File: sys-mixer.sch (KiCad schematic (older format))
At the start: 11 parts, among them J1 RCA L&R, J2 RCA L&R, J3 RCA L&R, SW1 4PDT

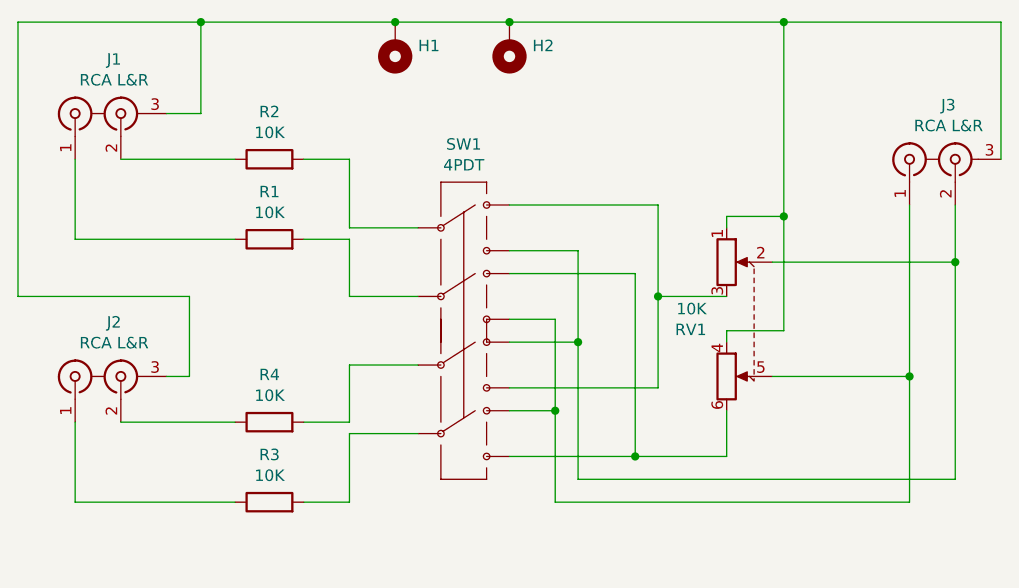
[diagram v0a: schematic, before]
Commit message: Fix resistor position in schematic
Having the resistors right after the inputs causes the mixing to
misbehave.

Also tweaked mounting hole and control positions, based on fitting of
2019-01-15 boards.
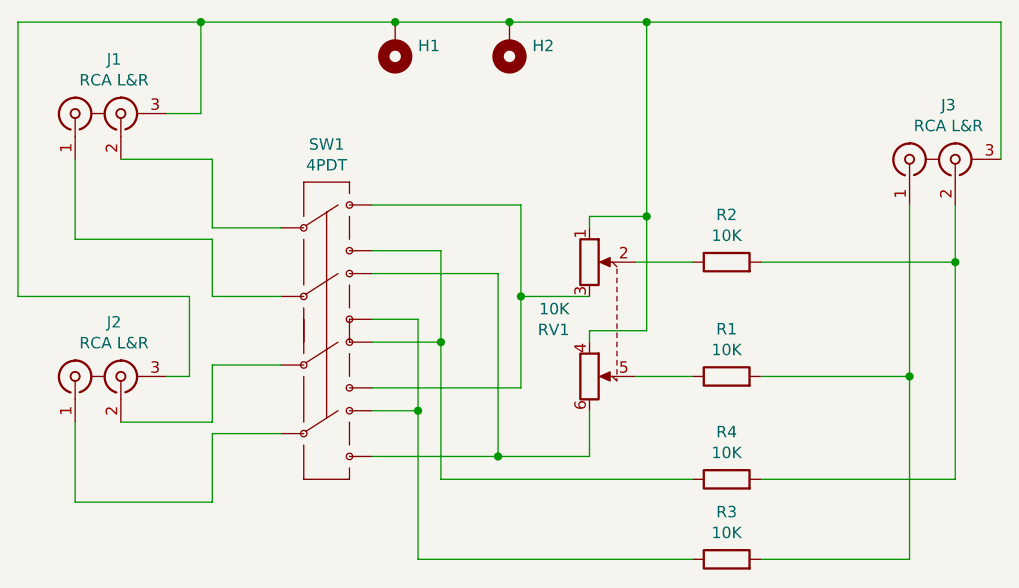
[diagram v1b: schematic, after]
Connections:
- net at J1.1 (IN1): now also SW1.6; no longer R1.1
- net at J1.2 (IN2): now also SW1.3; no longer R2.1
- net at J2.1 (IN1): now also SW1.12; no longer R3.1
- net at J2.2 (IN2): now also SW1.9; no longer R4.1
- net at SW1.10, SW1.5: now also R3.1; no longer J3.1 (IN1), RV1.5
- net at SW1.2, SW1.7: now also R4.1; no longer J3.2 (IN2), RV1.2
- net at R2.2: now also J3.2 (IN2), R4.2; no longer SW1.3
- net at R1.2: now also J3.1 (IN1), R3.2; no longer SW1.6
- new net: R2.1, RV1.2
- new net: R1.1, RV1.5
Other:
- moved on the sheet: R1, R2, R3, R4, RV1, SW1
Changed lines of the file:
@@
 EESchema Schematic File Version 4
+LIBS:sys-mixer-cache
 EELAYER 26 0
 EELAYER END
@@
 Sheet 1 1
 Title "SYS Mixer"
-Date "2019-01-15"
+Date "2019-01-26"
 Rev "0"
 Comp "Guano Audio Technologies"
@@
 L Device:R R2
 U 1 1 5C3BB760
-P 1900 1650
-F 0 "R2" V 2107 1650 50  0000 C CNN
-F 1 "10K" V 2016 1650 50  0000 C CNN
-F 2 "Resistor_THT:R_Axial_DIN0207_L6.3mm_D2.5mm_P10.16mm_Horizontal" V 1830 1650 50  0001 C CNN
-F 3 "/home/alex/Documents/pcb/sys-mixer/datasheets/mrs16m25-239694.pdf" H 1900 1650 50  0001 C CNN
-	1    1900 1650
+P 3900 2100
+F 0 "R2" V 4107 2100 50  0000 C CNN
+F 1 "10K" V 4016 2100 50  0000 C CNN
+F 2 "Resistor_THT:R_Axial_DIN0207_L6.3mm_D2.5mm_P10.16mm_Horizontal" V 3830 2100 50  0001 C CNN
+F 3 "/home/alex/Documents/pcb/sys-mixer/datasheets/mrs16m25-239694.pdf" H 3900 2100 50  0001 C CNN
+	1    3900 2100
 	0    -1   -1   0
 $EndComp
@@
 L Device:R R1
 U 1 1 5C3BB7F1
-P 1900 2000
-F 0 "R1" V 2107 2000 50  0000 C CNN
-F 1 "10K" V 2016 2000 50  0000 C CNN
-F 2 "Resistor_THT:R_Axial_DIN0207_L6.3mm_D2.5mm_P10.16mm_Horizontal" V 1830 2000 50  0001 C CNN
-F 3 "/home/alex/Documents/pcb/sys-mixer/datasheets/mrs16m25-239694.pdf" H 1900 2000 50  0001 C CNN
-	1    1900 2000
+P 3900 2600
+F 0 "R1" V 4107 2600 50  0000 C CNN
+F 1 "10K" V 4016 2600 50  0000 C CNN
+F 2 "Resistor_THT:R_Axial_DIN0207_L6.3mm_D2.5mm_P10.16mm_Horizontal" V 3830 2600 50  0001 C CNN
+F 3 "/home/alex/Documents/pcb/sys-mixer/datasheets/mrs16m25-239694.pdf" H 3900 2600 50  0001 C CNN
+	1    3900 2600
 	0    -1   -1   0
 $EndComp
@@
 L Device:R R4
 U 1 1 5C3BBB9D
-P 1900 2800
-F 0 "R4" V 2107 2800 50  0000 C CNN
-F 1 "10K" V 2016 2800 50  0000 C CNN
-F 2 "Resistor_THT:R_Axial_DIN0207_L6.3mm_D2.5mm_P10.16mm_Horizontal" V 1830 2800 50  0001 C CNN
-F 3 "/home/alex/Documents/pcb/sys-mixer/datasheets/mrs16m25-239694.pdf" H 1900 2800 50  0001 C CNN
-	1    1900 2800
+P 3900 3050
+F 0 "R4" V 4107 3050 50  0000 C CNN
+F 1 "10K" V 4016 3050 50  0000 C CNN
+F 2 "Resistor_THT:R_Axial_DIN0207_L6.3mm_D2.5mm_P10.16mm_Horizontal" V 3830 3050 50  0001 C CNN
+F 3 "/home/alex/Documents/pcb/sys-mixer/datasheets/mrs16m25-239694.pdf" H 3900 3050 50  0001 C CNN
+	1    3900 3050
 	0    -1   -1   0
 $EndComp
@@
 L Device:R R3
 U 1 1 5C3BBBA4
-P 1900 3150
-F 0 "R3" V 2107 3150 50  0000 C CNN
-F 1 "10K" V 2016 3150 50  0000 C CNN
-F 2 "Resistor_THT:R_Axial_DIN0207_L6.3mm_D2.5mm_P10.16mm_Horizontal" V 1830 3150 50  0001 C CNN
-F 3 "/home/alex/Documents/pcb/sys-mixer/datasheets/mrs16m25-239694.pdf" H 1900 3150 50  0001 C CNN
-	1    1900 3150
+P 3900 3400
+F 0 "R3" V 4107 3400 50  0000 C CNN
+F 1 "10K" V 4016 3400 50  0000 C CNN
+F 2 "Resistor_THT:R_Axial_DIN0207_L6.3mm_D2.5mm_P10.16mm_Horizontal" V 3830 3400 50  0001 C CNN
+F 3 "/home/alex/Documents/pcb/sys-mixer/datasheets/mrs16m25-239694.pdf" H 3900 3400 50  0001 C CNN
+	1    3900 3400
 	0    -1   -1   0
 $EndComp
@@
 L Device:R_POT_Dual RV1
 U 1 1 5C3BC3EF
-P 4000 2350
-F 0 "RV1" V 4046 2162 50  0000 R CNN
-F 1 "10K" V 3955 2162 50  0000 R CNN
-F 2 "extra-footprints:POT-RK09712200MC" H 4250 2275 50  0001 C CNN
-F 3 "/home/alex/Documents/pcb/sys-mixer/datasheets/RK097-1370742.pdf" H 4250 2275 50  0001 C CNN
-	1    4000 2350
+P 3400 2350
+F 0 "RV1" V 3446 2162 50  0000 R CNN
+F 1 "10K" V 3355 2162 50  0000 R CNN
+F 2 "extra-footprints:POT-RK09712200MC" H 3650 2275 50  0001 C CNN
+F 3 "/home/alex/Documents/pcb/sys-mixer/datasheets/RK097-1370742.pdf" H 3650 2275 50  0001 C CNN
+	1    3400 2350
 	0    1    1    0
 $EndComp
@@
 L SparkFun-Electromechanical:SWITCH-4PDTCNK_LOCK SW1
 U 1 1 5C3C1364
-P 2750 2450
-F 0 "SW1" H 2750 3315 50  0000 C CNN
-F 1 "4PDT" H 2750 3224 50  0000 C CNN
-F 2 "extra-footprints:4PDT-SPUN191400" H 2780 2600 20  0001 C CNN
-F 3 "/home/alex/Documents/pcb/sys-mixer/datasheets/SPUN-1370861.pdf" H 2750 2450 50  0001 C CNN
-	1    2750 2450
+P 2150 2450
+F 0 "SW1" H 2150 3315 50  0000 C CNN
+F 1 "4PDT" H 2150 3224 50  0000 C CNN
+F 2 "extra-footprints:4PDT-SPUN191400" H 2180 2600 20  0001 C CNN
+F 3 "/home/alex/Documents/pcb/sys-mixer/datasheets/SPUN-1370861.pdf" H 2150 2450 50  0001 C CNN
+	1    2150 2450
 	1    0    0    -1
 $EndComp
@@
 	800  1050 800  2250
 Wire Wire Line
-	2250 1950 2550 1950
-Wire Wire Line
-	2250 1650 2250 1950
-Wire Wire Line
-	2250 2250 2550 2250
-Wire Wire Line
-	2250 2000 2250 2250
-Wire Wire Line
-	2250 2800 2250 2550
-Wire Wire Line
-	2250 2550 2550 2550
-Wire Wire Line
-	2250 3150 2250 2850
-Wire Wire Line
-	2250 2850 2550 2850
+	1650 1950 1950 1950
+Wire Wire Line
+	1650 1650 1650 1950
+Wire Wire Line
+	1650 2250 1950 2250
+Wire Wire Line
+	1650 2000 1650 2250
+Wire Wire Line
+	1650 2800 1650 2550
+Wire Wire Line
+	1650 2550 1950 2550
+Wire Wire Line
+	1650 3150 1650 2850
+Wire Wire Line
+	1650 2850 1950 2850
 Wire Wire Line
 	800  1050 1600 1050
 Wire Wire Line
-	2050 3150 2250 3150
-Wire Wire Line
-	2050 2800 2250 2800
-Wire Wire Line
-	2050 1650 2250 1650
-Wire Wire Line
-	2050 2000 2250 2000
-Wire Wire Line
-	1250 1650 1750 1650
-Wire Wire Line
-	1050 2000 1750 2000
-Wire Wire Line
-	1250 2800 1750 2800
-Wire Wire Line
-	1050 3150 1750 3150
-Wire Wire Line
-	2950 2950 3500 2950
-Wire Wire Line
-	3900 2950 3900 2750
-Wire Wire Line
-	2950 2650 3600 2650
-Wire Wire Line
-	3600 2650 3600 2250
-Wire Wire Line
-	3600 2250 3900 2250
-Wire Wire Line
-	2950 2050 3250 2050
-Wire Wire Line
-	2950 2350 3150 2350
-Wire Wire Line
-	3150 2350 3150 2750
-Wire Wire Line
-	2950 2750 3150 2750
-Connection ~ 3150 2750
-Wire Wire Line
-	2950 1850 3600 1850
-Wire Wire Line
-	3600 1850 3600 2250
-Connection ~ 3600 2250
-Wire Wire Line
-	2950 2150 3500 2150
-Wire Wire Line
-	3500 2150 3500 2950
-Connection ~ 3500 2950
-Wire Wire Line
-	3500 2950 3900 2950
-Wire Wire Line
-	3250 2050 3250 2450
-Connection ~ 3250 2450
-Wire Wire Line
-	3250 2450 3250 3050
-Wire Wire Line
-	2950 2450 3250 2450
-Wire Wire Line
-	3900 2450 3900 2400
-Wire Wire Line
-	3900 1950 3900 1900
-Wire Wire Line
-	3150 3150 4700 3150
-Wire Wire Line
-	3900 2400 4150 2400
-Wire Wire Line
-	4150 1050 4150 1900
-Wire Wire Line
-	3900 1900 4150 1900
-Connection ~ 4150 1900
-Wire Wire Line
-	4150 1900 4150 2400
-Wire Wire Line
-	4150 1050 5100 1050
-Connection ~ 4150 1050
-Wire Wire Line
-	3150 2750 3150 3150
-Wire Wire Line
-	3250 3050 4900 3050
+	2350 2950 2900 2950
+Wire Wire Line
+	3300 2950 3300 2750
+Wire Wire Line
+	3000 2250 3300 2250
+Wire Wire Line
+	2350 2050 2650 2050
+Wire Wire Line
+	2350 2350 2550 2350
+Wire Wire Line
+	2550 2350 2550 2750
+Wire Wire Line
+	2350 2750 2550 2750
+Connection ~ 2550 2750
+Wire Wire Line
+	2350 2150 2900 2150
+Wire Wire Line
+	2900 2150 2900 2950
+Connection ~ 2900 2950
+Wire Wire Line
+	2650 2050 2650 2450
+Connection ~ 2650 2450
+Wire Wire Line
+	2650 2450 2650 3050
+Wire Wire Line
+	2350 2450 2650 2450
+Wire Wire Line
+	3300 2450 3300 2400
+Wire Wire Line
+	3300 1950 3300 1900
+Wire Wire Line
+	3300 2400 3550 2400
+Wire Wire Line
+	3550 1050 3550 1900
+Wire Wire Line
+	3300 1900 3550 1900
+Connection ~ 3550 1900
+Wire Wire Line
+	3550 1900 3550 2400
 Wire Wire Line
 	5100 1050 5100 1650
@@
 Connection ~ 2950 1050
 Wire Wire Line
-	2950 1050 4150 1050
+	3500 2600 3750 2600
+Wire Wire Line
+	3500 2100 3750 2100
+Wire Wire Line
+	1250 1650 1650 1650
+Wire Wire Line
+	1050 2000 1650 2000
+Wire Wire Line
+	1250 2800 1650 2800
+Wire Wire Line
+	1050 3150 1650 3150
+Wire Wire Line
+	2950 1050 3550 1050
+Wire Wire Line
+	2350 1850 3000 1850
+Wire Wire Line
+	2350 2650 3000 2650
+Wire Wire Line
+	2900 2950 3300 2950
+Wire Wire Line
+	3000 1850 3000 2250
+Wire Wire Line
+	3000 2250 3000 2650
+Connection ~ 3000 2250
+Connection ~ 3550 1050
+Wire Wire Line
+	4900 1850 4900 2100
+Wire Wire Line
+	3550 1050 5100 1050
+Wire Wire Line
+	2650 3050 3750 3050
+Wire Wire Line
+	2550 3400 3750 3400
+Wire Wire Line
+	2550 2750 2550 3400
+Wire Wire Line
+	4050 3050 4900 3050
+Wire Wire Line
+	4050 3400 4700 3400
 Wire Wire Line
 	4700 1850 4700 2600
 Wire Wire Line
-	4100 2100 4900 2100
-Wire Wire Line
-	4900 1850 4900 2100
+	4050 2100 4900 2100
+Wire Wire Line
+	4900 2100 4900 3050
 Connection ~ 4900 2100
 Wire Wire Line
-	4900 2100 4900 3050
-Wire Wire Line
-	4100 2600 4700 2600
+	4050 2600 4700 2600
+Wire Wire Line
+	4700 2600 4700 3400
 Connection ~ 4700 2600
-Wire Wire Line
-	4700 2600 4700 3150
 $EndSCHEMATC
